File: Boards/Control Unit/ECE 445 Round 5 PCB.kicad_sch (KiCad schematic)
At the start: 48 parts, among them J1 Screw_Terminal_01x12, J10 Screw_Terminal_01x03, J11 Screw_Terminal_01x12, J12 Screw_Terminal_01x03, J13 Screw_Terminal_01x03, J14 Screw_Terminal_01x03, J15 Screw_Terminal_01x03, J16 Screw_Terminal_01x03, J17 Screw_Terminal_01x03, J18 Screw_Terminal_01x03, J19 Screw_Terminal_01x03, J20 Conn_ARM_JTAG_SWD_10, J27 Screw_Terminal_01x12, J28 Screw_Terminal_01x12, J3 Screw_Terminal_01x03, J4 Screw_Terminal_01x03, J5 Screw_Terminal_01x03, J6 Screw_Terminal_01x03, J7 Conn_02x03_Odd_Even, J9 Screw_Terminal_01x03, Q1 NMOS, Q10 NMOS, Q11 NMOS, Q12 NMOS, Q2 NMOS, Q3 NMOS, Q4 NMOS, Q5 NMOS, Q6 NMOS, Q7 NMOS, Q8 NMOS, Q9 NMOS, SW1 SW_Push, U1 STM32F401RBTx

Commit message: control unit ERC Changes part 1
resistors need changes
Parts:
- added J2, J21, J8: Screw_Terminal_01x03, Connector_PinSocket_2.54mm:PinSocket_1x03_P2.54mm_Vertical, symbol Connector:Screw_Terminal_01x03
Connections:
- net D- is gone; now on net T11: U1.44 (PA11)
- net +3.3V: now also J21.1 (Pin_1), J21.2 (Pin_2), J21.3 (Pin_3)
- net +5V: now also J2.1 (Pin_1), J2.2 (Pin_2), J2.3 (Pin_3)
- net GND: now also J8.1 (Pin_1), J8.2 (Pin_2), J8.3 (Pin_3)
- net T11: no longer U1.40 (PC9)
- net D+: no longer names the net of U1.45 (PA12)
- no-connect marks 0 -> 21
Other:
- moved on the sheet: C17, C18, J20, J7, JP1, Q1, Q10, Q11, Q12, Q2, Q3, Q4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

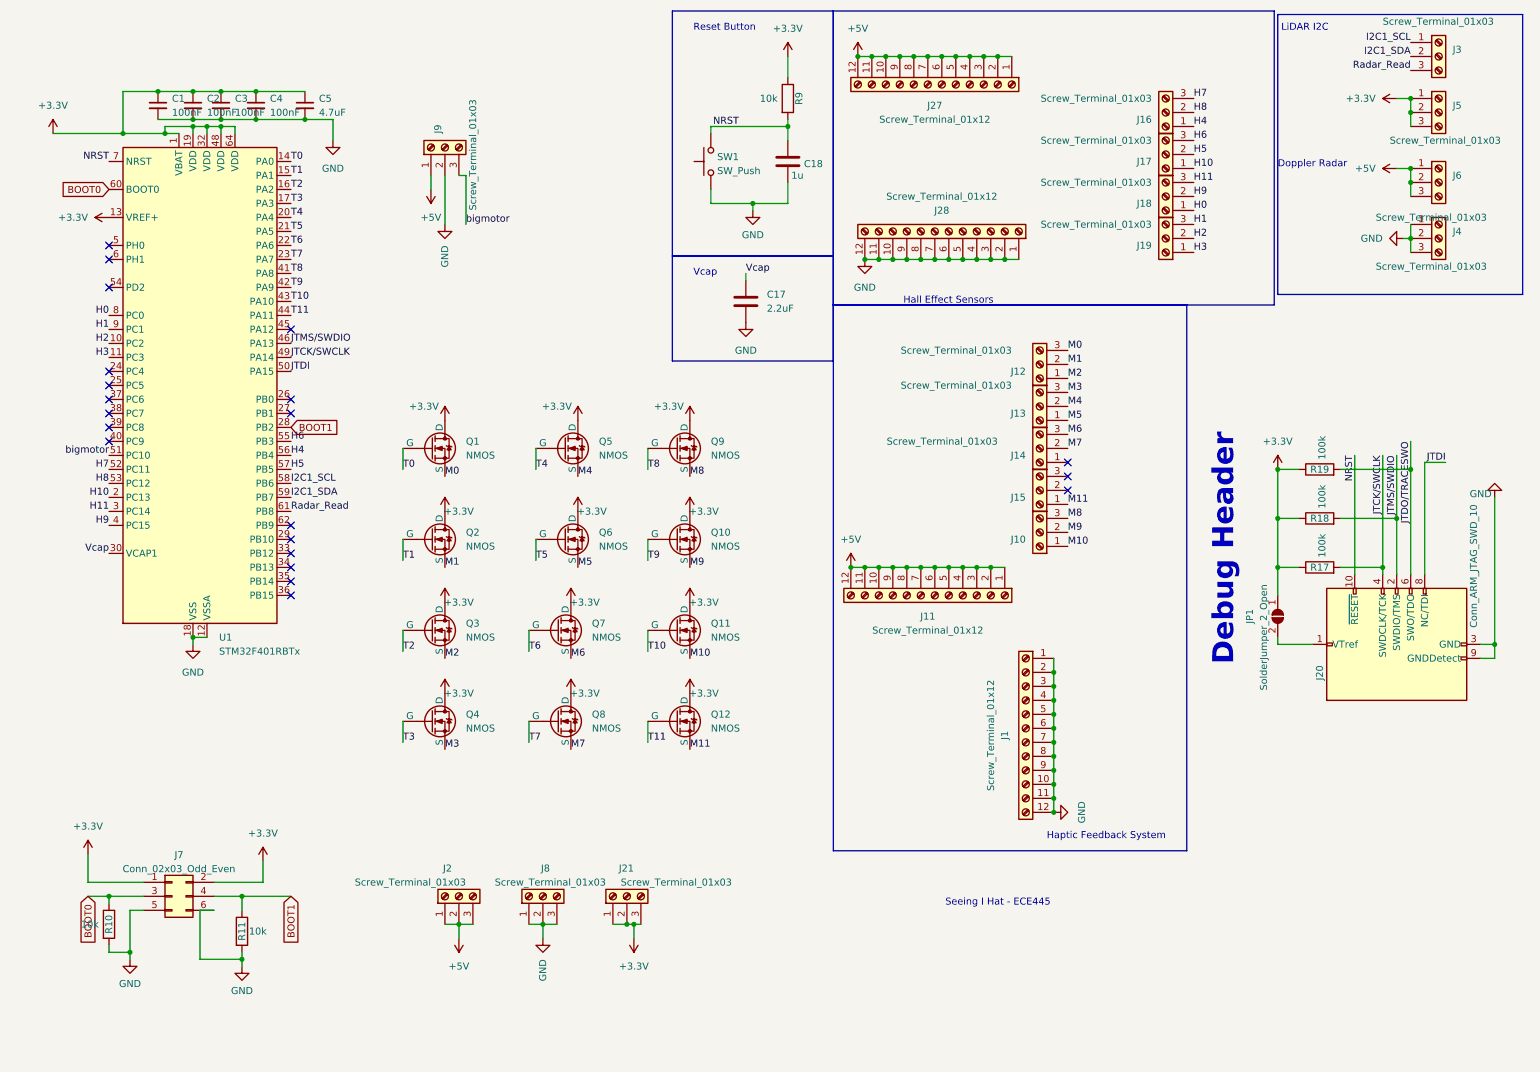
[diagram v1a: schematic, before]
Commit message: control unit pt2 all errors/warnings fixed
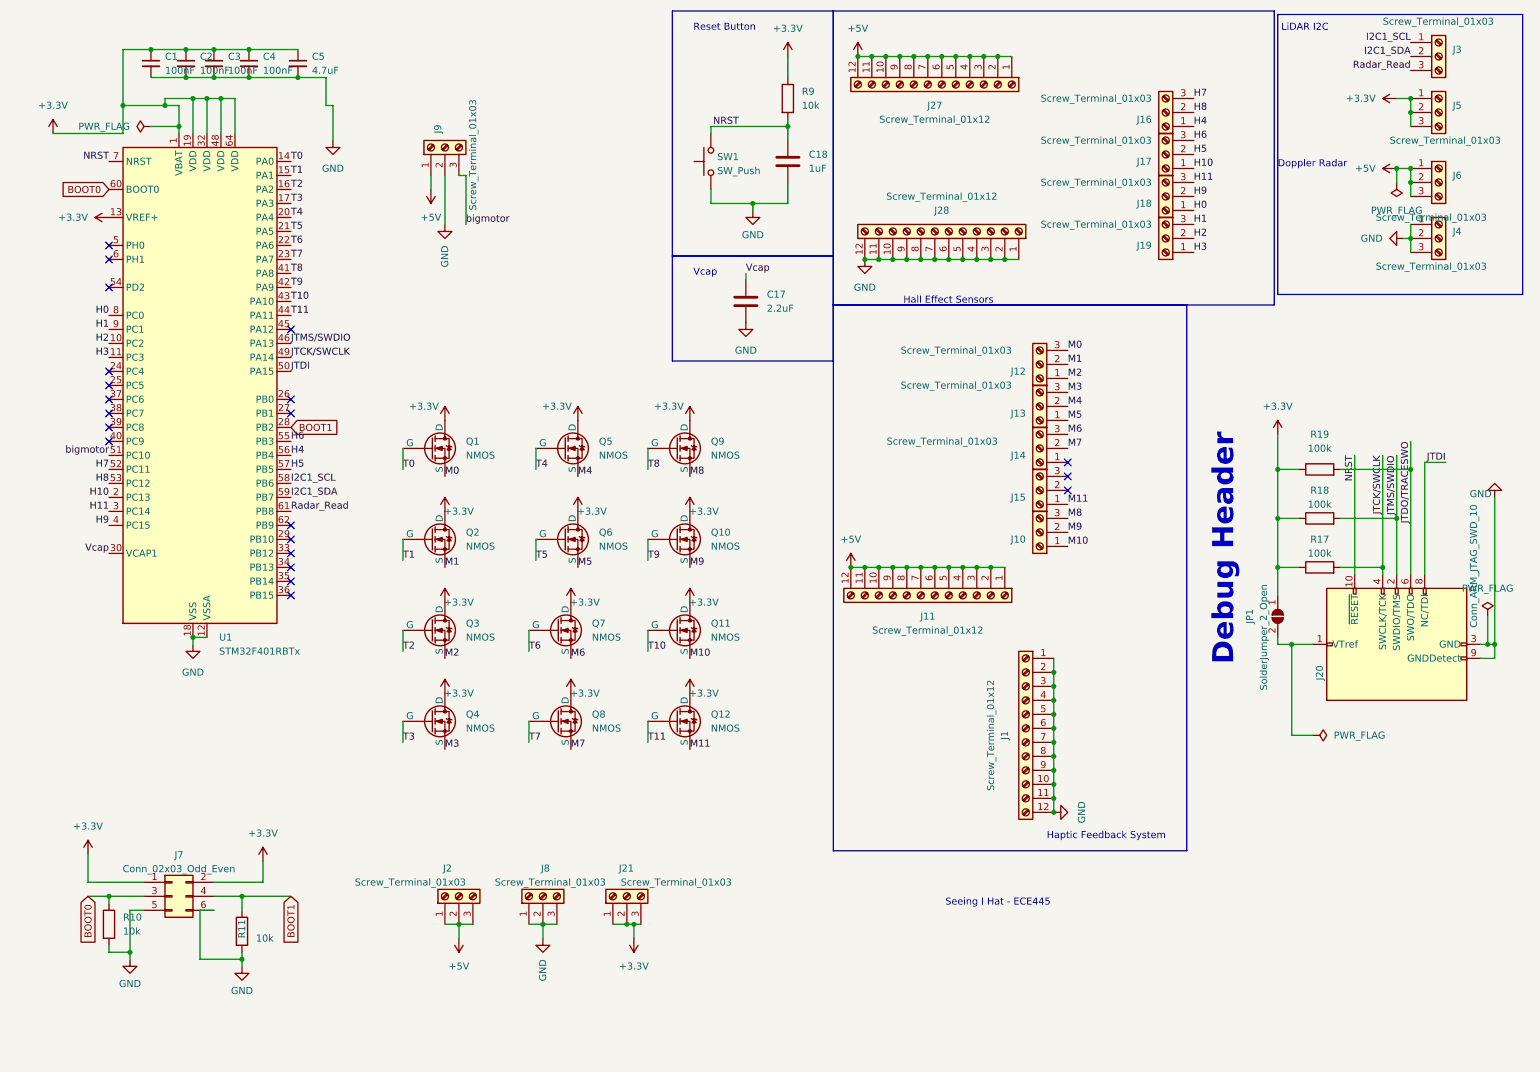
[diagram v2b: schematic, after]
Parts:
- removed C18: 1u, Capacitor_SMD:C_0805_2012Metric_Pad1.18x1.45mm_HandSolder, symbol basic:C
- removed R10, R11, R9: 10k, Resistor_SMD:R_0805_2012Metric_Pad1.20x1.40mm_HandSolder, symbol basic:R
- removed R17, R18, R19: 100k, Resistor_SMD:R_0805_2012Metric_Pad1.20x1.40mm_HandSolder, symbol basic:R
- added C18: 1uF, Capacitor_SMD:C_0805_2012Metric_Pad1.18x1.45mm_HandSolder, symbol Device:C
- added R10, R11, R9: 10k, Resistor_SMD:R_0805_2012Metric_Pad1.20x1.40mm_HandSolder, symbol Device:R
- added R17, R18, R19: 100k, Resistor_SMD:R_0805_2012Metric_Pad1.20x1.40mm_HandSolder, symbol Device:R
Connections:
- net +3.3V: now also R17.1, R18.1, R19.1, R9.1
- net BOOT0: now also R10.1
- net BOOT1: now also R11.1
- net GND: now also C18.2, R10.2, R11.2
- net JTCK/SWCLK: now also R17.2
- net JTDO/TRACESWO: now also R19.2
- net JTMS/SWDIO: now also R18.2
- net NRST: now also C18.1, R9.2
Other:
- moved on the sheet: C1, C2, C3, C4, C5

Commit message: removed extranious 5v power buses
hall effect module is pretty nice
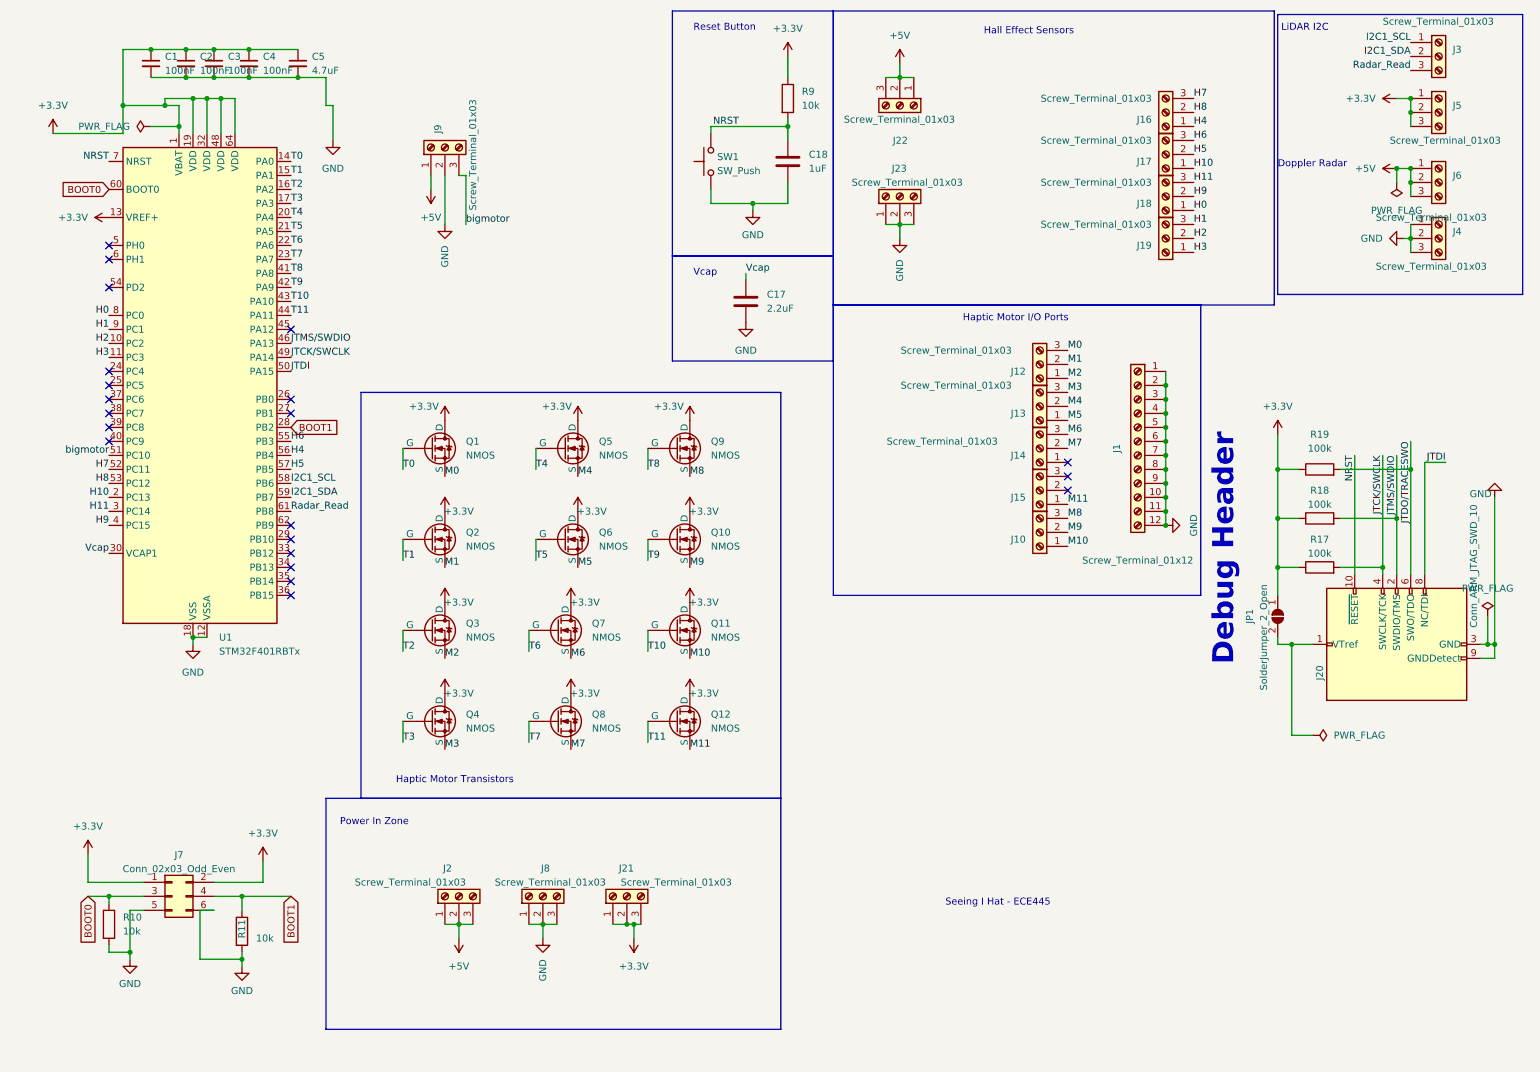
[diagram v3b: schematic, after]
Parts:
- removed J11, J27, J28: Screw_Terminal_01x12, Connector_PinSocket_2.54mm:PinSocket_1x12_P2.54mm_Vertical, symbol Connector:Screw_Terminal_01x12
- added J22, J23: Screw_Terminal_01x03, Connector_PinSocket_2.54mm:PinSocket_1x03_P2.54mm_Vertical, symbol Connector:Screw_Terminal_01x03
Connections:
- net +5V: now also J22.1 (Pin_1), J22.2 (Pin_2), J22.3 (Pin_3)
- net GND: now also J23.1 (Pin_1), J23.2 (Pin_2), J23.3 (Pin_3)
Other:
- note added: "Haptic Motor I/O Ports"
- note added: "Haptic Motor Transistors"
- note added: "Power In Zone"
- note removed: "Haptic Feedback System"
- moved on the sheet: J1

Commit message: routed except gnd and vcc
that was rough
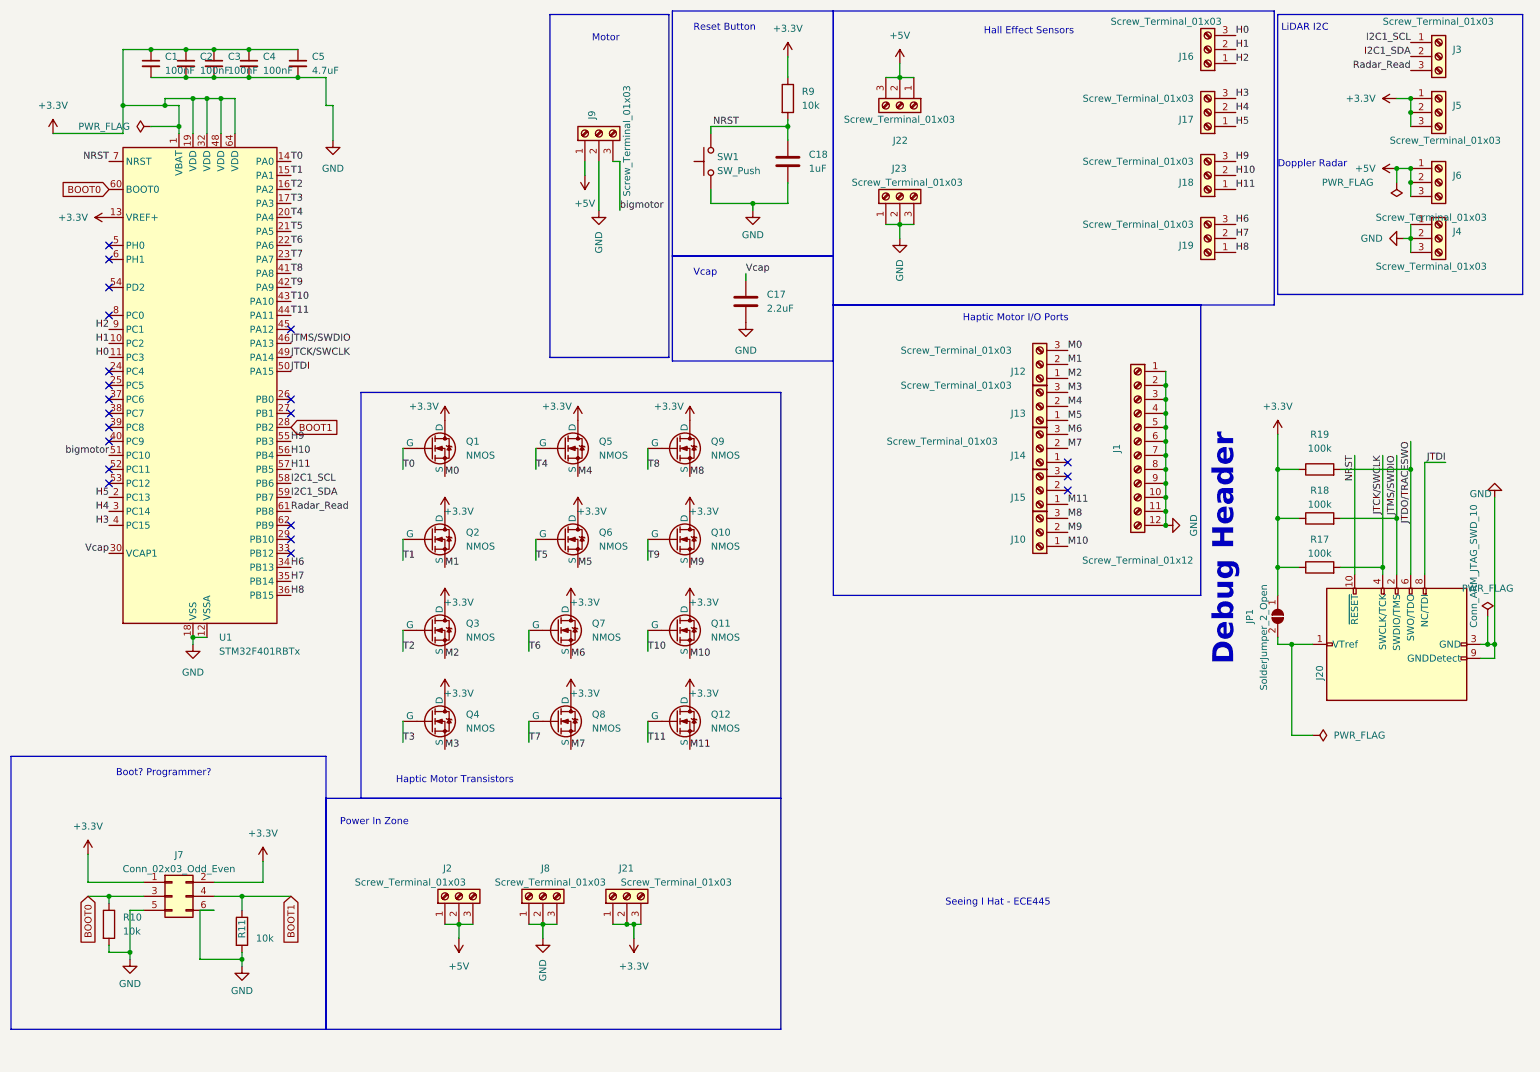
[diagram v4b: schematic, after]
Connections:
- net H0: now also J16.3 (Pin_3), U1.11 (PC3); no longer J18.1 (Pin_1), U1.8 (PC0)
- net H1: now also J16.2 (Pin_2), U1.10 (PC2); no longer J19.3 (Pin_3), U1.9 (PC1)
- net H10: now also J18.2 (Pin_2), U1.56 (PB4); no longer J17.1 (Pin_1), U1.2 (PC13)
- net H11: now also J18.1 (Pin_1), U1.57 (PB5); no longer J18.3 (Pin_3), U1.3 (PC14)
- net H2: now also J16.1 (Pin_1), U1.9 (PC1); no longer J19.2 (Pin_2), U1.10 (PC2)
- net H3: now also J17.3 (Pin_3), U1.4 (PC15); no longer J19.1 (Pin_1), U1.11 (PC3)
- net H4: now also J17.2 (Pin_2), U1.3 (PC14); no longer J16.1 (Pin_1), U1.56 (PB4)
- net H5: now also J17.1 (Pin_1), U1.2 (PC13); no longer J17.2 (Pin_2), U1.57 (PB5)
- net H6: now also J19.3 (Pin_3), U1.34 (PB13); no longer J17.3 (Pin_3), U1.55 (PB3)
- net H7: now also J19.2 (Pin_2), U1.35 (PB14); no longer J16.3 (Pin_3), U1.52 (PC11)
- net H8: now also J19.1 (Pin_1), U1.36 (PB15); no longer J16.2 (Pin_2), U1.53 (PC12)
- net H9: now also J18.3 (Pin_3), U1.55 (PB3); no longer J18.2 (Pin_2), U1.4 (PC15)
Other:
- note added: "Boot? Programmer?"
- note added: "Motor"
- moved on the sheet: J16, J17, J18, J19, J9
